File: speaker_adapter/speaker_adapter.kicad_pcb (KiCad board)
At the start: 2 copper layers, 15 x 6 mm, 4 parts, among them J1 SPK_P, J2 SPK_N, J3 SPK_P, J4 SPK_N

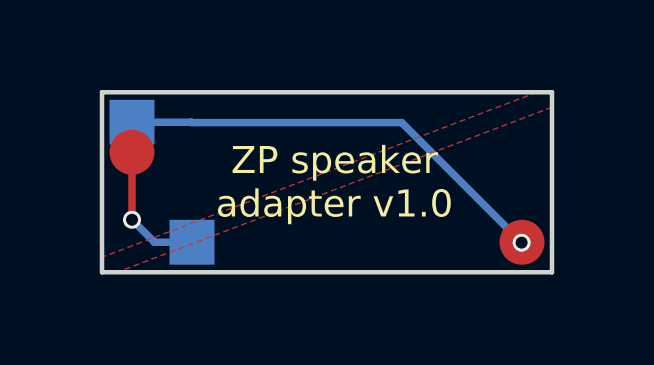
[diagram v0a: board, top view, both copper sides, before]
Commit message: Updated speaker adapter to better reflect reality
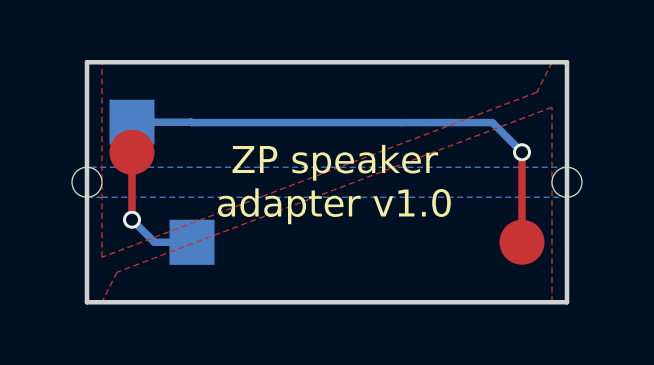
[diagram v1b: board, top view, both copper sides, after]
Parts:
- added TP1: TEST, Measurement_Points:Measurement_Point_Round-TH_Small, F.Cu at (134.5, 88.0)
- added TP2: TEST, Measurement_Points:Measurement_Point_Round-TH_Small, F.Cu at (150.5, 88.0)
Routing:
- net Net-(J2-Pad1): track 14.7 -> 16.4 mm
- added copper zone on B.Cu, net Net-(J1-Pad1)
- added copper zone on B.Cu, net Net-(J2-Pad1)
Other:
- board size 15 x 6 mm -> 16 x 8 mm
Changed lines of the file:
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@@
     (links 2)
     (no_connects 0)
-    (area 134.924999 84.924999 150.075001 91.075001)
+    (area 134.424999 83.924999 150.575001 92.075001)
     (thickness 0.8)
     (drawings 5)
-    (tracks 10)
+    (tracks 12)
     (zones 0)
-    (modules 4)
+    (modules 6)
     (nets 3)
   )
@@
     (44 Edge.Cuts user)
     (45 Margin user)
-    (46 B.CrtYd user)
+    (46 B.CrtYd user hide)
     (47 F.CrtYd user)
     (48 B.Fab user hide)
@@
     (last_trace_width 0.25)
     (trace_clearance 0.2)
-    (zone_clearance 0.508)
+    (zone_clearance 0.2)
     (zone_45_only no)
     (trace_min 0.2)
@@
     (fp_line (start 1 -1) (end -1 -1) (layer B.CrtYd) (width 0.05))
     (fp_line (start -1 -1) (end -1 1) (layer B.CrtYd) (width 0.05))
-    (pad 1 smd rect (at 0 0) (size 1.5 1.5) (layers B.Cu B.Mask)
+    (pad 1 smd rect (at 0 0) (size 1.5 1.5) (layers B.Cu)
       (net 1 "Net-(J1-Pad1)"))
   )
@@
     (fp_line (start 1 -1) (end -1 -1) (layer B.CrtYd) (width 0.05))
     (fp_line (start -1 -1) (end -1 1) (layer B.CrtYd) (width 0.05))
-    (pad 1 smd rect (at 0 0) (size 1.5 1.5) (layers B.Cu B.Mask)
+    (pad 1 smd rect (at 0 0) (size 1.5 1.5) (layers B.Cu)
       (net 2 "Net-(J2-Pad1)"))
   )
@@
       (net 2 "Net-(J2-Pad1)"))
   )
+  (module Measurement_Points:Measurement_Point_Round-TH_Small (layer F.Cu)
+    (at 134.5 88)
+    (descr "Mesurement Point, Square, Trough Hole,  DM 1.5mm, Drill 0.8mm,")
+    (tags "Mesurement Point Round Trough Hole 1.5mm Drill 0.8mm")
+    (attr virtual)
+    (fp_text reference TP1 (at 0 -2) (layer F.SilkS) hide
+      (effects (font (size 1 1) (thickness 0.15)))
+    )
+    (fp_text value TEST (at 0 2) (layer F.Fab)
+      (effects (font (size 1 1) (thickness 0.15)))
+    )
+    (fp_circle (center 0 0) (end 1 0) (layer F.CrtYd) (width 0.05))
+    (pad "" np_thru_hole circle (at 0 0) (size 1 1) (drill 1) (layers *.Cu))
+  )
+  (module Measurement_Points:Measurement_Point_Round-TH_Small (layer F.Cu)
+    (at 150.5 88)
+    (descr "Mesurement Point, Square, Trough Hole,  DM 1.5mm, Drill 0.8mm,")
+    (tags "Mesurement Point Round Trough Hole 1.5mm Drill 0.8mm")
+    (attr virtual)
+    (fp_text reference TP2 (at 0 -2) (layer F.SilkS) hide
+      (effects (font (size 1 1) (thickness 0.15)))
+    )
+    (fp_text value TEST (at 0 2) (layer F.Fab)
+      (effects (font (size 1 1) (thickness 0.15)))
+    )
+    (fp_circle (center 0 0) (end 1 0) (layer F.CrtYd) (width 0.05))
+    (pad "" np_thru_hole circle (at 0 0) (size 1 1) (drill 1) (layers *.Cu))
+  )
   (gr_text "ZP speaker\nadapter v1.0" (at 142.75 88) (layer F.SilkS)
     (effects (font (size 0.9 0.9) (thickness 0.17)))
   )
-  (gr_line (start 150 85) (end 135 85) (layer Edge.Cuts) (width 0.15))
-  (gr_line (start 150 91) (end 150 85) (layer Edge.Cuts) (width 0.15))
-  (gr_line (start 135 91) (end 150 91) (layer Edge.Cuts) (width 0.15))
-  (gr_line (start 135 85) (end 135 91) (layer Edge.Cuts) (width 0.15))
+  (gr_line (start 150.5 84) (end 134.5 84) (layer Edge.Cuts) (width 0.15))
+  (gr_line (start 150.5 92) (end 150.5 84) (layer Edge.Cuts) (width 0.15))
+  (gr_line (start 134.5 92) (end 150.5 92) (layer Edge.Cuts) (width 0.15))
+  (gr_line (start 134.5 84) (end 134.5 92) (layer Edge.Cuts) (width 0.15))
   (segment (start 136 89.250002) (end 136 87) (width 0.25) (layer F.Cu) (net 1))
   (segment (start 138 90) (end 136.749998 90) (width 0.25) (layer B.Cu) (net 1))
   (segment (start 136.749998 90) (end 136 89.250002) (width 0.25) (layer B.Cu) (net 1))
   (via (at 136 89.250002) (size 0.6) (drill 0.4) (layers F.Cu B.Cu) (net 1))
+  (segment (start 149 87) (end 149 90) (width 0.25) (layer F.Cu) (net 2))
+  (segment (start 144.991202 86.011465) (end 148.011465 86.011465) (width 0.25) (layer B.Cu) (net 2))
+  (segment (start 148.011465 86.011465) (end 149 87) (width 0.25) (layer B.Cu) (net 2))
+  (via (at 149 87) (size 0.6) (drill 0.4) (layers F.Cu B.Cu) (net 2))
+  (segment (start 137.988535 86.011465) (end 144.991202 86.011465) (width 0.25) (layer B.Cu) (net 2))
+  (segment (start 148.987181 90.007444) (end 148.987181 90.013186) (width 0.25) (layer B.Cu) (net 2))
+  (segment (start 137.97707 86) (end 137.988535 86.011465) (width 0.25) (layer B.Cu) (net 2))
   (segment (start 136 86) (end 137.97707 86) (width 0.25) (layer B.Cu) (net 2))
-  (segment (start 137.97707 86) (end 137.988535 86.011465) (width 0.25) (layer B.Cu) (net 2))
-  (segment (start 137.988535 86.011465) (end 144.991202 86.011465) (width 0.25) (layer B.Cu) (net 2))
-  (segment (start 144.991202 86.011465) (end 148.987181 90.007444) (width 0.25) (layer B.Cu) (net 2))
-  (segment (start 148.987181 90.007444) (end 148.987181 90.013186) (width 0.25) (layer B.Cu) (net 2))
-  (via (at 148.987181 90.013186) (size 0.6) (drill 0.4) (layers F.Cu B.Cu) (net 2))
   (zone (net 1) (net_name "Net-(J1-Pad1)") (layer F.Cu) (hatch edge 0.508)
     (connect_pads yes (clearance 0.2))
@@
     (polygon
       (pts
-        (xy 135 85) (xy 149.5 85) (xy 135 90.5)
+        (xy 135 84) (xy 150 84) (xy 149.5 85) (xy 135 90.5)
       )
     )
@@
     (polygon
       (pts
-        (xy 150 85.5) (xy 135.5 91) (xy 150 91)
+        (xy 150 85.5) (xy 135.5 91) (xy 135 92) (xy 150 92)
       )
     )
@@
     (polygon
       (pts
-        (xy 136.5 85) (xy 149.5 85) (xy 145.5 86.5) (xy 136.5 86.5)
+        (xy 136.5 84) (xy 150 84) (xy 149.5 85) (xy 145.5 86.5) (xy 136.5 86.5)
       )
     )
@@
     (polygon
       (pts
-        (xy 139.5 89.5) (xy 148.5 89.5) (xy 148.5 91) (xy 135.5 91)
+        (xy 139.5 89.5) (xy 148.5 89.5) (xy 148.5 92) (xy 135 92) (xy 135.5 91)
       )
     )
@@
       )
     )
+  )
+  (zone (net 1) (net_name "Net-(J1-Pad1)") (layer B.Cu) (hatch edge 0.508)
+    (connect_pads yes (clearance 0.2))
+    (min_thickness 0.2)
+    (fill yes (arc_segments 16) (thermal_gap 0.2) (thermal_bridge_width 0.24))
+    (polygon
+      (pts
+        (xy 135 88.5) (xy 150.5 88.5) (xy 150.5 92) (xy 134.5 92) (xy 134.5 88.5)
+      )
+    )
+  )
+  (zone (net 2) (net_name "Net-(J2-Pad1)") (layer B.Cu) (hatch edge 0.508)
+    (connect_pads yes (clearance 0.2))
+    (min_thickness 0.2)
+    (fill yes (arc_segments 16) (thermal_gap 0.2) (thermal_bridge_width 0.24))
+    (polygon
+      (pts
+        (xy 134.5 84) (xy 150.5 84) (xy 150.5 87.5) (xy 134.5 87.5)
+      )
+    )
+  )
+  (zone (net 0) (net_name "") (layer B.Mask) (hatch edge 0.508)
+    (connect_pads yes (clearance 0.2))
+    (min_thickness 0.2)
+    (fill yes (arc_segments 16) (thermal_gap 0.2) (thermal_bridge_width 0.24))
+    (polygon
+      (pts
+        (xy 134.5 86) (xy 140 86) (xy 140 87.5) (xy 134.5 87.5)
+      )
+    )
+  )
+  (zone (net 0) (net_name "") (layer B.Mask) (hatch edge 0.508)
+    (connect_pads yes (clearance 0.2))
+    (min_thickness 0.2)
+    (fill yes (arc_segments 16) (thermal_gap 0.2) (thermal_bridge_width 0.24))
+    (polygon
+      (pts
+        (xy 134.5 88.5) (xy 140 88.5) (xy 140 90) (xy 134.5 90)
+      )
+    )

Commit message: Speaker adapter v1.1 - edge holes adjusted for 1.6mm PCBs
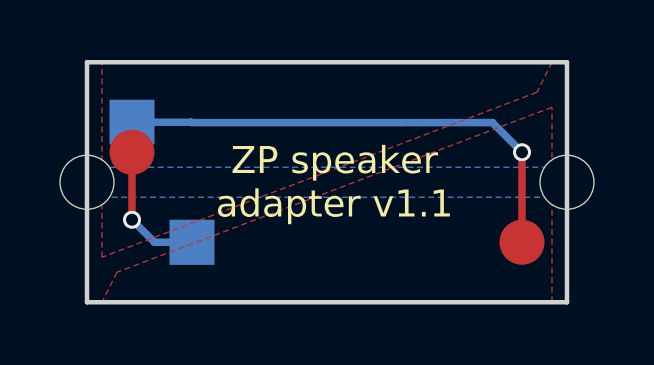
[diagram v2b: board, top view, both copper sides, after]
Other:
- board text added: "ZP speaker adapter v1.1"
- board text removed: "ZP speaker adapter v1.0"
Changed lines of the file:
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@@
     (mod_text_size 1 1)
     (mod_text_width 0.15)
-    (pad_size 1.5 1.5)
-    (pad_drill 0)
+    (pad_size 1.8 1.8)
+    (pad_drill 1.8)
     (pad_to_mask_clearance 0.2)
     (aux_axis_origin 150.5 84.5)
@@
     )
     (fp_circle (center 0 0) (end 1 0) (layer F.CrtYd) (width 0.05))
-    (pad "" np_thru_hole circle (at 0 0) (size 1 1) (drill 1) (layers *.Cu))
+    (pad "" np_thru_hole circle (at 0 0) (size 1.8 1.8) (drill 1.8) (layers *.Cu))
   )
   (module Measurement_Points:Measurement_Point_Round-TH_Small (layer F.Cu)
@@
     )
     (fp_circle (center 0 0) (end 1 0) (layer F.CrtYd) (width 0.05))
-    (pad "" np_thru_hole circle (at 0 0) (size 1 1) (drill 1) (layers *.Cu))
+    (pad "" np_thru_hole circle (at 0 0) (size 1.8 1.8) (drill 1.8) (layers *.Cu))
   )
-  (gr_text "ZP speaker\nadapter v1.0" (at 142.75 88) (layer F.SilkS)
+  (gr_text "ZP speaker\nadapter v1.1" (at 142.75 88) (layer F.SilkS)
     (effects (font (size 0.9 0.9) (thickness 0.17)))
   )
@@
   (gr_line (start 134.5 92) (end 150.5 92) (layer Edge.Cuts) (width 0.15))
   (gr_line (start 134.5 84) (end 134.5 92) (layer Edge.Cuts) (width 0.15))
+  (segment (start 148.987181 90.007444) (end 148.987181 90.013186) (width 0.25) (layer B.Cu) (net 0))
   (segment (start 136 89.250002) (end 136 87) (width 0.25) (layer F.Cu) (net 1))
   (segment (start 138 90) (end 136.749998 90) (width 0.25) (layer B.Cu) (net 1))
@@
   (via (at 149 87) (size 0.6) (drill 0.4) (layers F.Cu B.Cu) (net 2))
   (segment (start 137.988535 86.011465) (end 144.991202 86.011465) (width 0.25) (layer B.Cu) (net 2))
-  (segment (start 148.987181 90.007444) (end 148.987181 90.013186) (width 0.25) (layer B.Cu) (net 2))
   (segment (start 137.97707 86) (end 137.988535 86.011465) (width 0.25) (layer B.Cu) (net 2))
   (segment (start 136 86) (end 137.97707 86) (width 0.25) (layer B.Cu) (net 2))
